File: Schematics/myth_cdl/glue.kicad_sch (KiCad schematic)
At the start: 6 parts, among them U10 74HC00, U3 74LS32, U5 74LS08, U6 74HC04, U7 74HC02, U8 74HC74

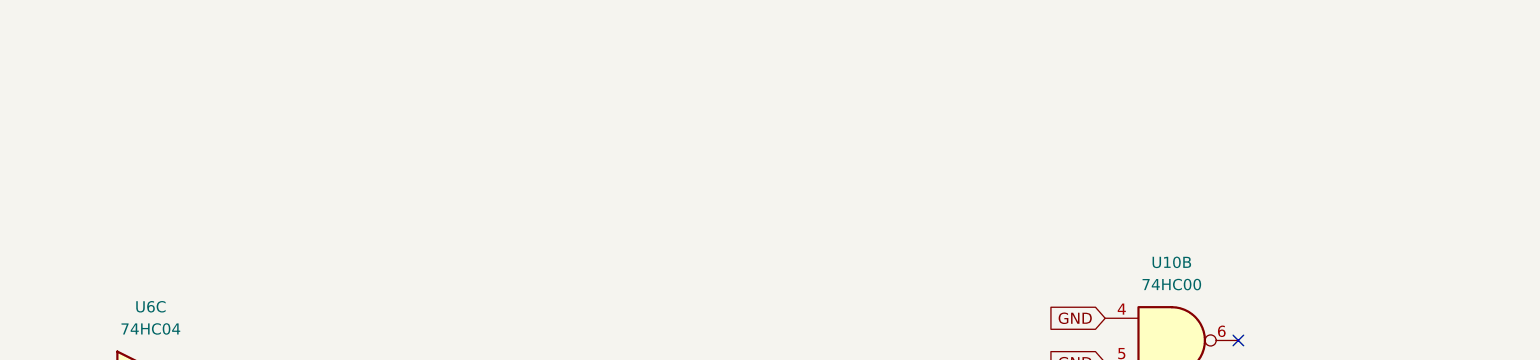
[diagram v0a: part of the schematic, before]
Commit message: Change d to g
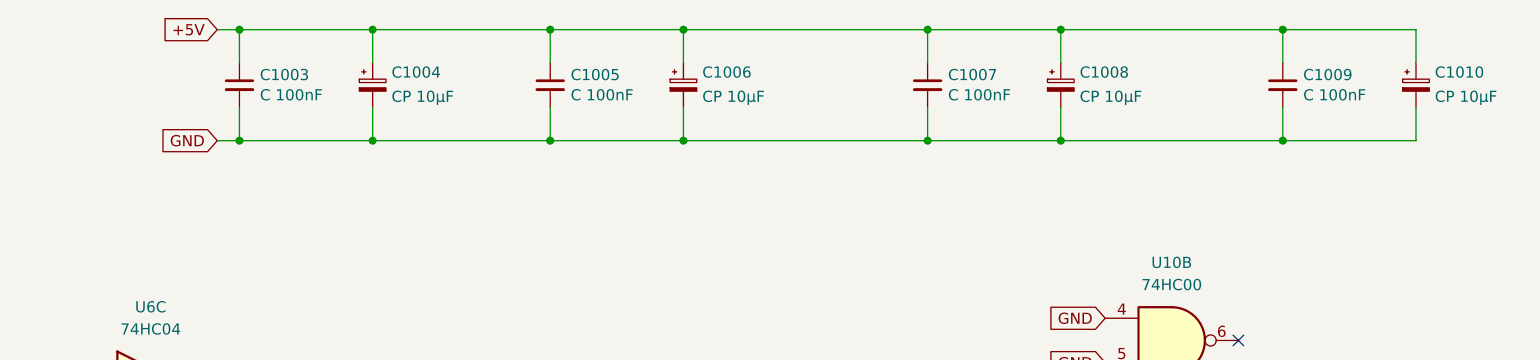
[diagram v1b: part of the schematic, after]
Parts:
- added C1003, C1005, C1007, C1009: C 100nF, Capacitor_THT:C_Disc_D5.0mm_W2.5mm_P2.50mm, symbol Device:C_Small
- added C1004, C1006, C1008, C1010: CP 10μF, Capacitor_THT:CP_Radial_D6.3mm_P2.50mm, symbol Device:C_Polarized_Small
- U10, U3, U5, U6, U7, U8: footprint (none) -> Package_DIP:DIP-14_W7.62mm_LongPads
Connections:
- net +5V: now also C1003.1, C1004.1, C1005.1, C1006.1, C1007.1, C1008.1, C1009.1, C1010.1
- net GND: now also C1003.2, C1004.2, C1005.2, C1006.2, C1007.2, C1008.2, C1009.2, C1010.2
